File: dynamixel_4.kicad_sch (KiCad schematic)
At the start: 25 parts, among them J6 Pico5, J7 Pico5, J8 Dynamixel-4, J9 Dynamixel-4, Q2 MMBT3906, U6 CH343P, U7 SIT3088E

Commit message: [update] Positionning v1
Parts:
- D13, D14: value B5819WS -> DNP - B5819WS; now not fitted
- J8, J9: value Dynamixel-4 -> DNP - Dynamixel-4; now not fitted
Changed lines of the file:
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@@
 	(title_block
 		(title "elec_maroilles")
-		(date "2025-11-26")
+		(date "2025-11-28")
 		(rev "A1")
 		(company "Pollen Robotics / Hugging Face")
@@
 		(in_bom yes)
 		(on_board yes)
-		(dnp no)
+		(dnp yes)
 		(property "Reference" "J9"
 			(at 325.374 200.152 0)
@@
 			)
 		)
-		(property "Value" "Dynamixel-4"
+		(property "Value" "DNP - Dynamixel-4"
 			(at 325.12 203.2001 0)
 			(effects
@@
 		(in_bom yes)
 		(on_board yes)
-		(dnp no)
+		(dnp yes)
 		(property "Reference" "D13"
 			(at 286.004 188.468 90)
@@
 			)
 		)
-		(property "Value" "B5819WS"
+		(property "Value" "DNP - B5819WS"
 			(at 284.48 192.7224 90)
 			(effects
@@
 		(in_bom yes)
 		(on_board yes)
-		(dnp no)
+		(dnp yes)
 		(property "Reference" "D14"
 			(at 293.116 188.468 90)
@@
 			)
 		)
-		(property "Value" "B5819WS"
+		(property "Value" "DNP - B5819WS"
 			(at 294.64 192.7224 90)
 			(effects
@@
 		(in_bom yes)
 		(on_board yes)
-		(dnp no)
+		(dnp yes)
 		(property "Reference" "J8"
 			(at 325.374 174.752 0)
@@
 			)
 		)
-		(property "Value" "Dynamixel-4"
+		(property "Value" "DNP - Dynamixel-4"
 			(at 325.12 177.8001 0)
 			(effects

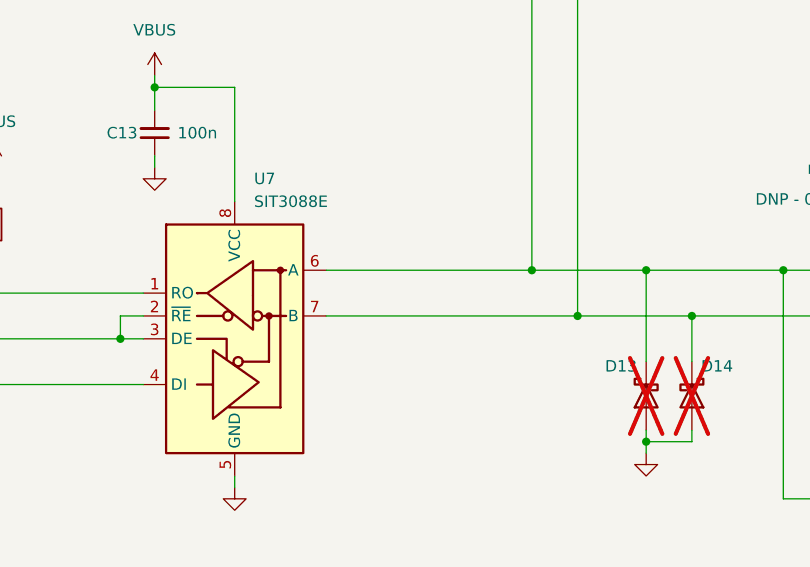
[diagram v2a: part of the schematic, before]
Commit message: [error] To be fixed: inverted diff pairs on grippers pico5.
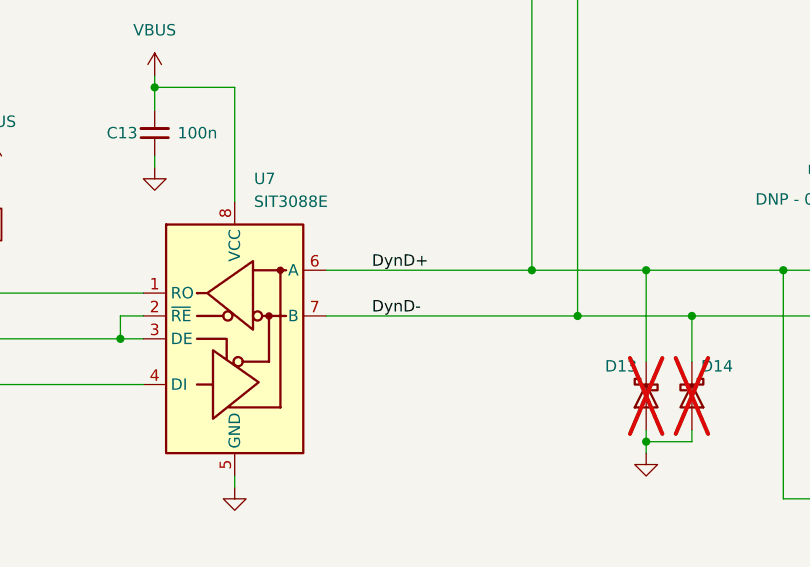
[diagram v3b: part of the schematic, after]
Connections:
- net DynD+: now reaches D13.1 (K), D15.1 (K), J6.4 (Pin_4), J7.4 (Pin_4), J8.3 (Pin_3), J9.3 (Pin_3), U7.6 (A)
- net DynD-: now reaches D14.1 (K), D16.1 (K), J6.5 (Pin_5), J7.5 (Pin_5), J8.4 (Pin_4), J9.4 (Pin_4), U7.7 (B)
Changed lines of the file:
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@@
+		)
+	)
+	(label "DynD+"
+		(at 256.54 177.8 0)
+		(effects
+			(font
+				(size 1.27 1.27)
+			)
+			(justify left bottom)
 		)
 	)
@@
 		(effects
 			(font
+				(size 1.27 1.27)
+			)
+			(justify left bottom)
+		)
+	)
+	(label "DynD-"
+		(at 256.54 182.88 0)
+		(effects
+			(font

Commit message: [update] Release B1!
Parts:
- C11, C9: LCSC Part C302042 -> C1592
- D15, D16: FT Rotation Offset 180 -> (none)
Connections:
- net DynD+: now also J6.2 (Pin_2), J7.2 (Pin_2); no longer J6.4 (Pin_4), J7.4 (Pin_4)
- net DynD-: now also J6.3 (Pin_3), J7.3 (Pin_3); no longer J6.5 (Pin_5), J7.5 (Pin_5)
- net USB_gripperM: now also J7.5 (Pin_5); no longer J7.3 (Pin_3)
- net USB_gripperP: now also J7.4 (Pin_4); no longer J7.2 (Pin_2)
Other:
- moved on the sheet: D12
